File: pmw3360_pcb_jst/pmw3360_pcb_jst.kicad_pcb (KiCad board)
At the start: 2 copper layers, 27 x 28 mm, 20 parts, among them J1 Conn_01x08, U1 PMW3360DM-T2QU, U2 TPS73601DBV

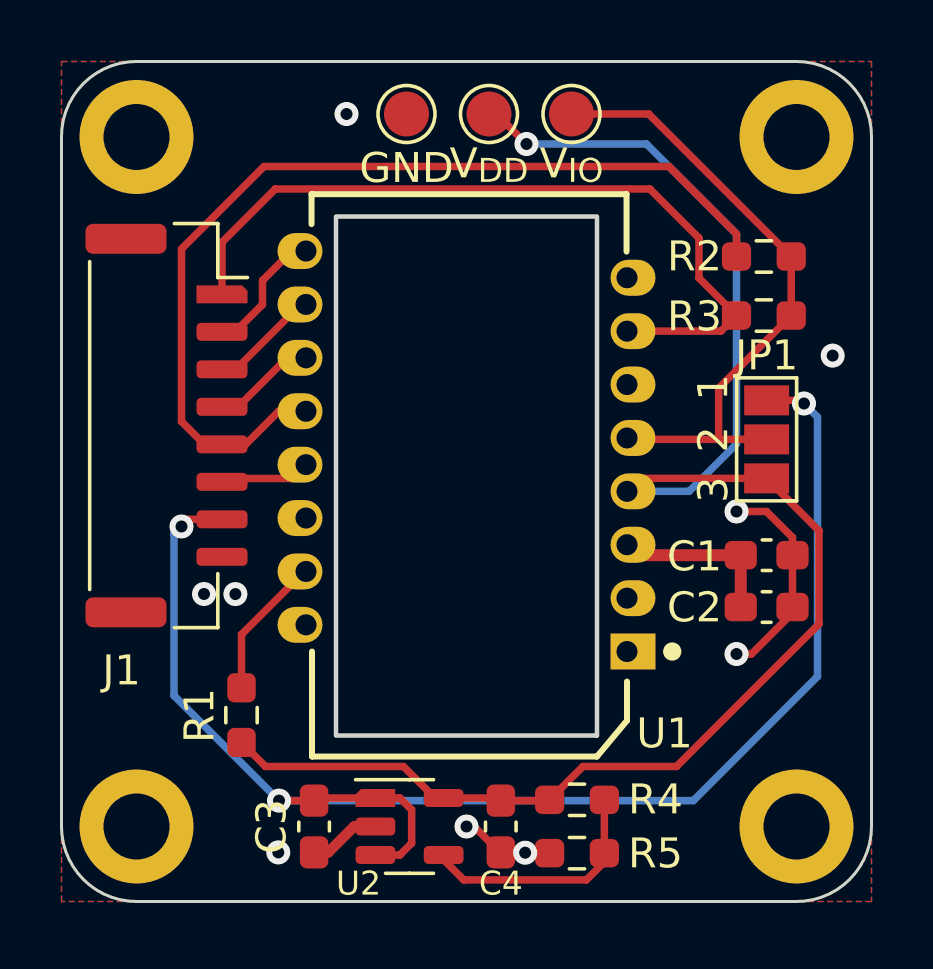
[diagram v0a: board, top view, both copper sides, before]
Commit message: Update symbol references
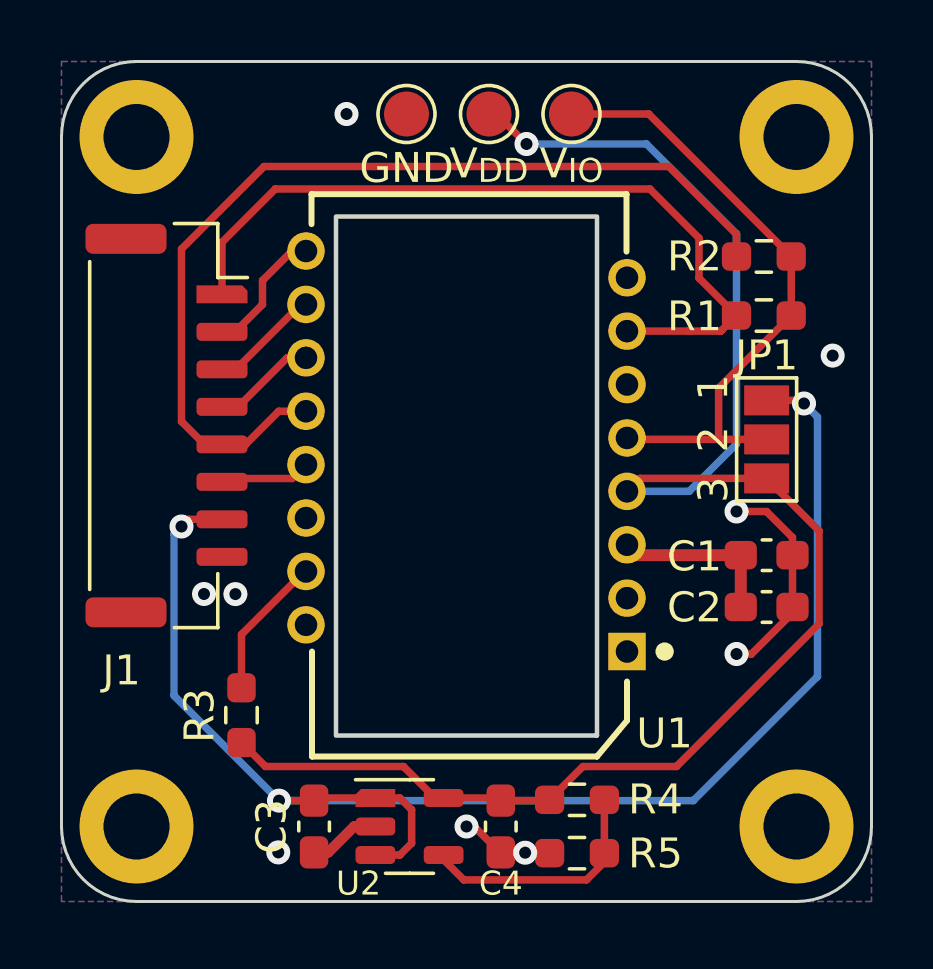
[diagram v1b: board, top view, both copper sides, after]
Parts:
- R1: renamed from R3; value DNI -> 10k
- R4: value Adj_R1 -> 28k
- R5: value Adj_R2 -> 56.2k
- TP1: value VIO TestPoint -> V_{IO}
- TP2: value VDD TestPoint -> V_{DD}
- TP3: value GND TestPoint -> GND
- renumbered R1 to R3
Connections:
- net V_IN renamed V_{IN}
- net V_IO renamed V_{IO}
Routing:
- net V_{IN}: track 50.2 -> 49.5 mm
